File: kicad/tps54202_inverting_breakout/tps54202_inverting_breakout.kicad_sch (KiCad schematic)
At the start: 23 parts, among them J1 Conn_01x04, J3 ENABLE, U1 TPS54202DDC

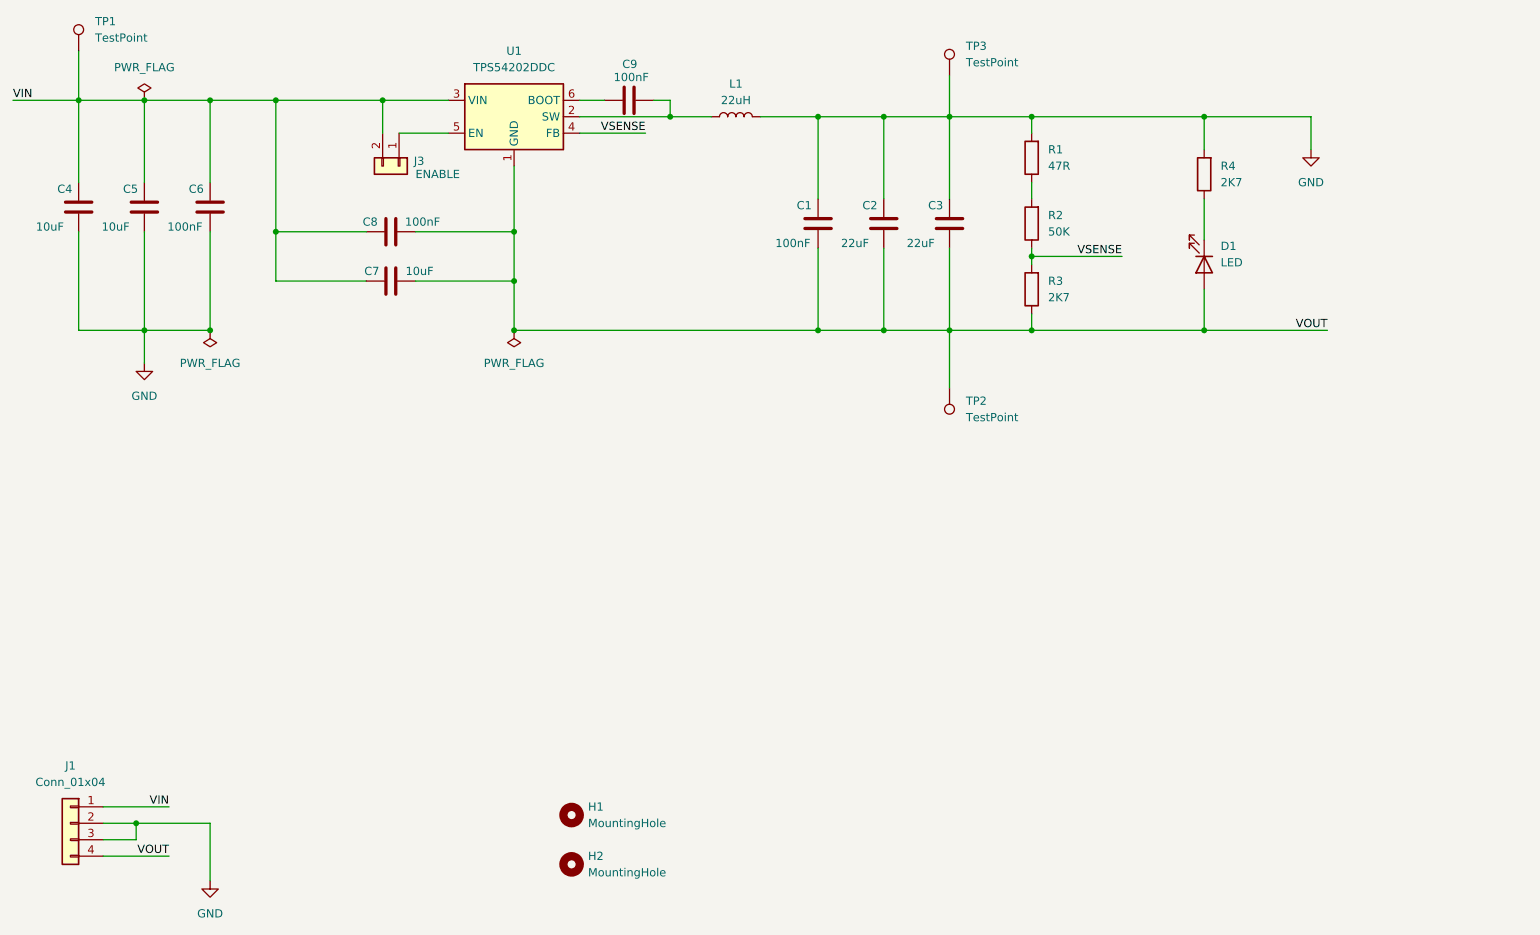
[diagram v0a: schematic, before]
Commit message: RevB layout, added outut caps, tighter bypass coupling, improved layout
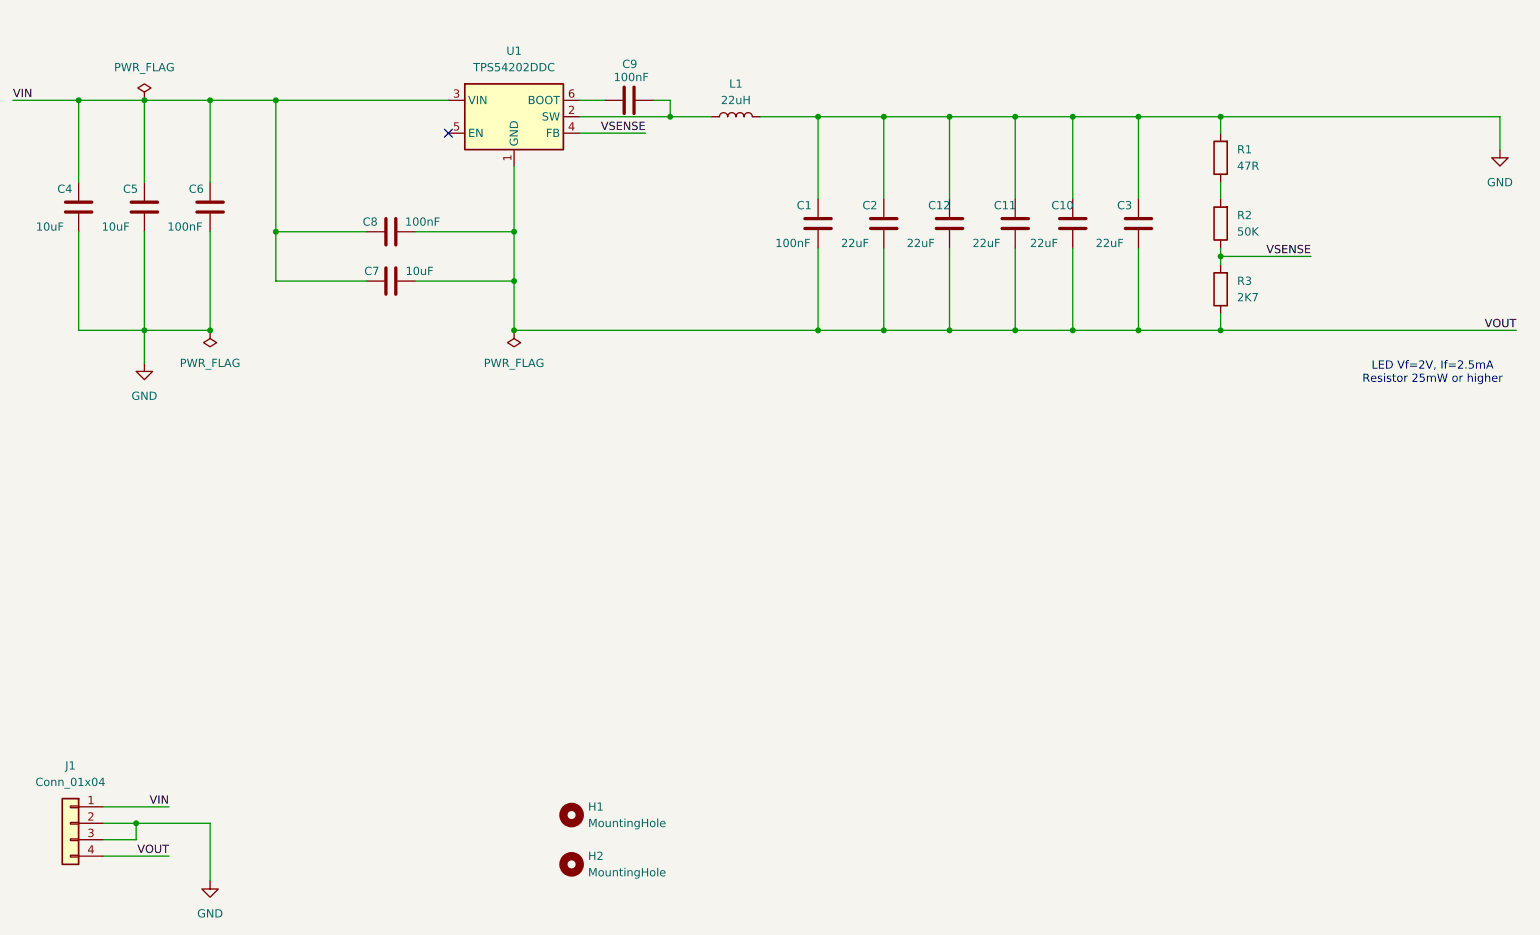
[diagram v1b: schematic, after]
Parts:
- removed D1: LED, LED_SMD:LED_1206_3216Metric_Pad1.42x1.75mm_HandSolder, symbol Device:LED
- removed J3: ENABLE, Connector_PinHeader_2.54mm:PinHeader_1x02_P2.54mm_Vertical, symbol Connector_Generic:Conn_01x02
- removed R4: 2K7, Resistor_SMD:R_0805_2012Metric_Pad1.20x1.40mm_HandSolder, symbol Device:R
- removed TP1, TP2: TestPoint, TestPoint:TestPoint_Pad_2.5x2.5mm, symbol Connector:TestPoint
- removed TP3: TestPoint, TestPoint:TestPoint_Keystone_5005-5009_Compact, symbol Connector:TestPoint
- added C10, C11, C12: 22uF, Capacitor_SMD:C_0805_2012Metric_Pad1.18x1.45mm_HandSolder, symbol Device:C
- C2, C3, C4, C5, C7: footprint Capacitor_SMD:CP_Elec_4x3 -> Capacitor_SMD:C_0805_2012Metric_Pad1.18x1.45mm_HandSolder
- L1: footprint Inductor_SMD:L_Ferrocore_DLG-0403 -> Inductor_SMD:L_Bourns-SRN8040_8x8.15mm
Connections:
- net GND: now also C10.1, C11.1, C12.1
- net VOUT: now also C10.2, C11.2, C12.2
- no-connect marks 0 -> 1
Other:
- note added: "LED Vf=2V, If=2.5mA Resistor 25mW or higher"
- moved on the sheet: C3, R1, R2, R3
